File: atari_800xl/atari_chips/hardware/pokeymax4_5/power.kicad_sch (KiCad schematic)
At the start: 15 parts

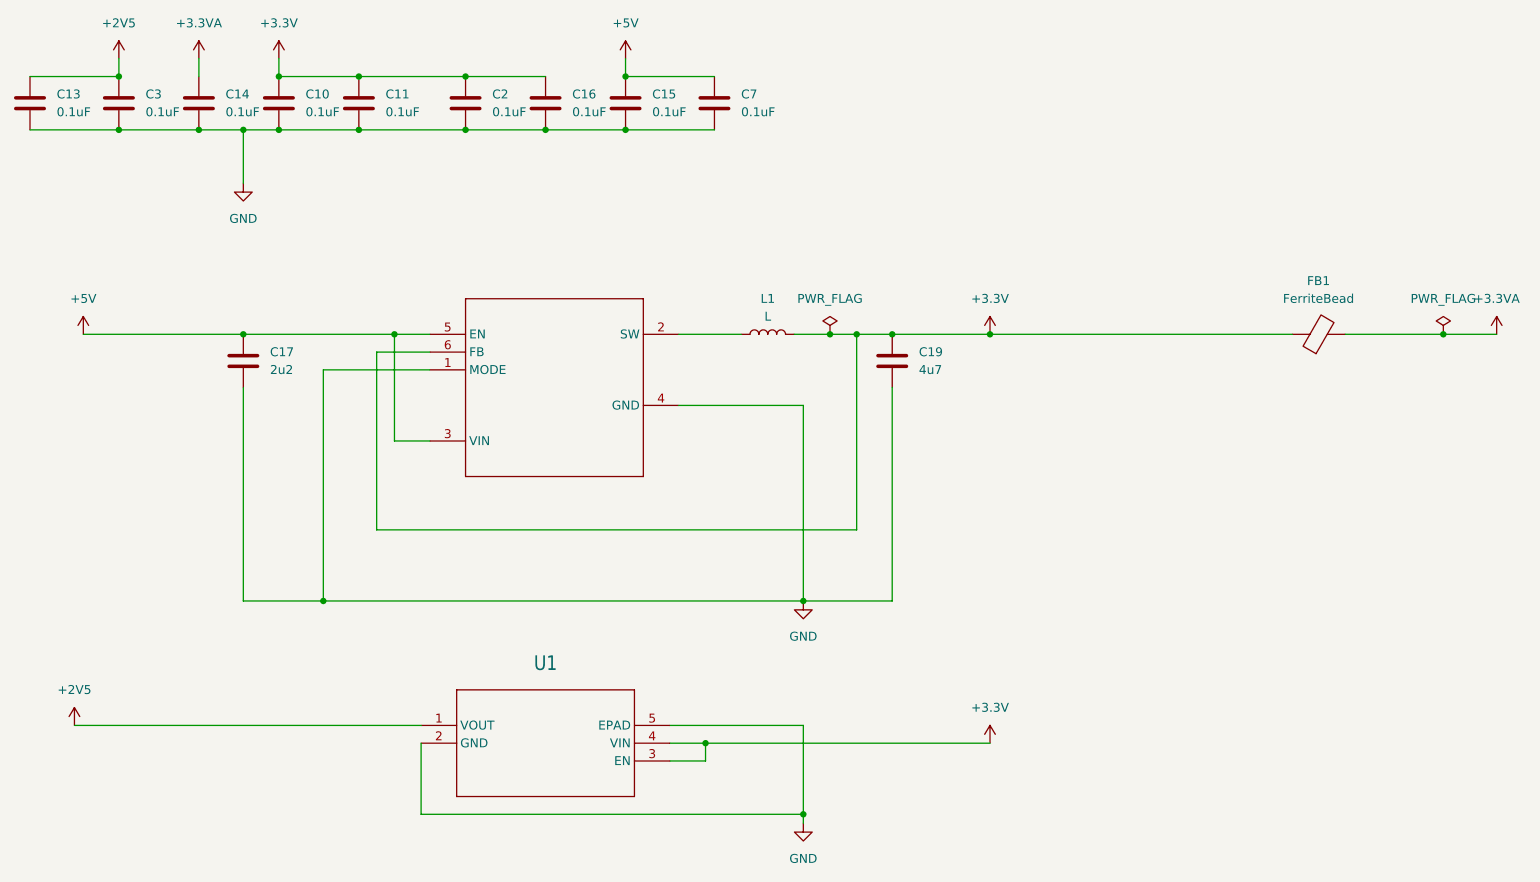
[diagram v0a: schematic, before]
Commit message: Pokeymax v4_53 as produced
git-svn-id: svn+ssh://192.168.0.3/home/svnfpga/repo/trunk@1512 d6161ac3-aae1-4d52-9b05-ea9ac36b53d3
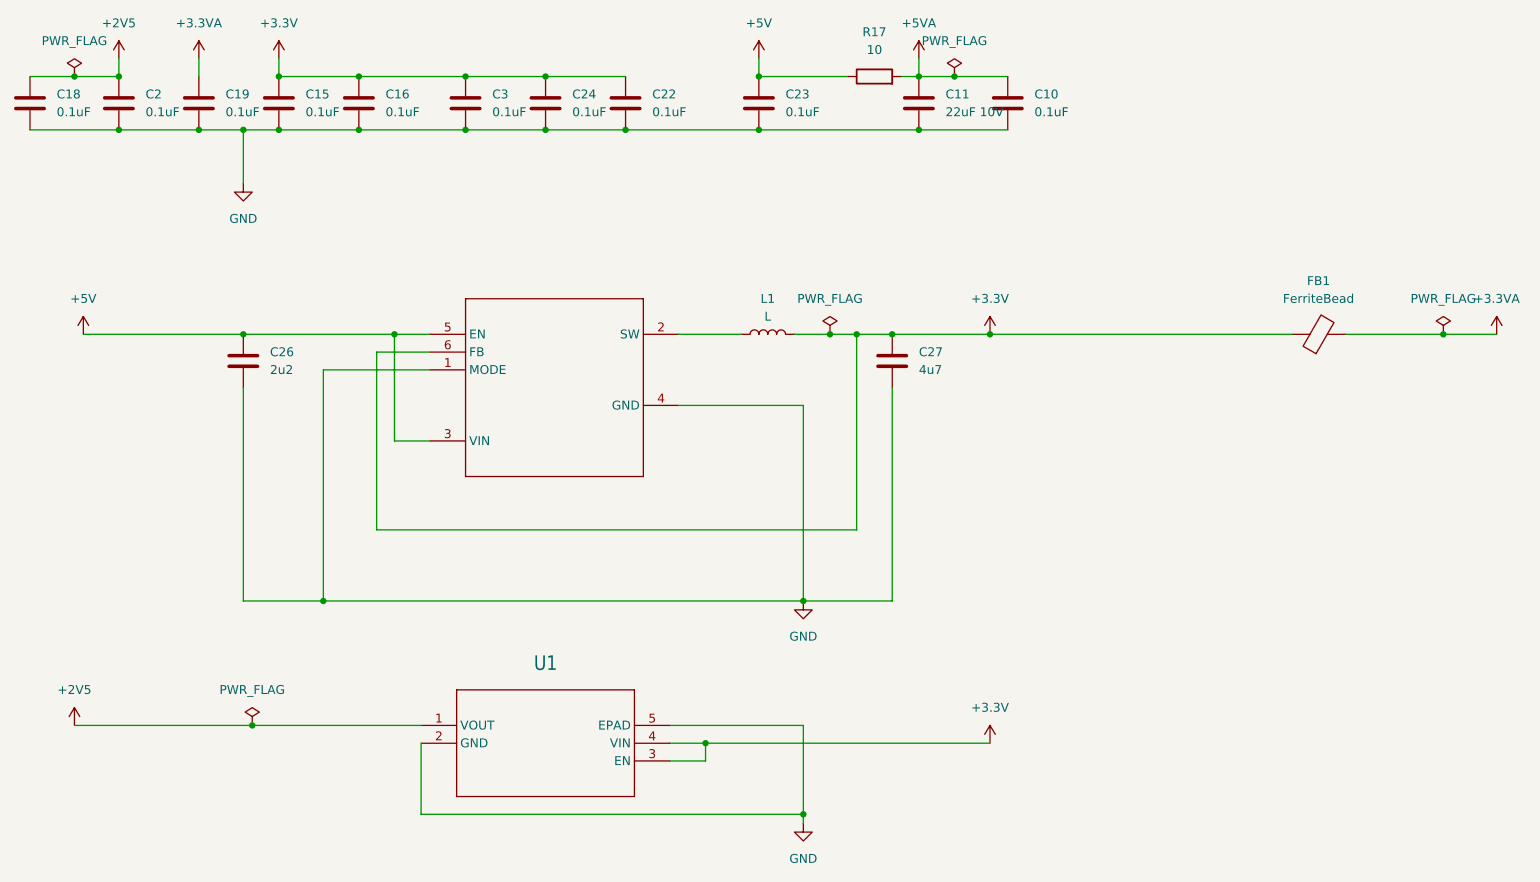
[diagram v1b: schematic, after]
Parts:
- removed C7: 0.1uF, Capacitor_SMD:C_0603_1608Metric, symbol Device:C
- added C10: 0.1uF, Capacitor_SMD:C_0402_1005Metric, symbol Device:C
- added C11: 22uF 10V, Capacitor_SMD:C_0603_1608Metric, symbol Device:C
- added C22: 0.1uF, Capacitor_SMD:C_0603_1608Metric, symbol Device:C
- added R17: 10, Resistor_SMD:R_0603_1608Metric, symbol Device:R
- renumbered C10 to C15, C11 to C16, C13 to C18, C14 to C19, C3 to C2, C15 to C23, C16 to C24, C17 to C26, C19 to C27, C2 to C3
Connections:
- net +3.3V: now also C22.1
- net +5V: now also R17.1
- net GND: now also C10.2, C11.2, C22.2
- new net +5VA: C10.1, C11.1, R17.2
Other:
- moved on the sheet: C23
